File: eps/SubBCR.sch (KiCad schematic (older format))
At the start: 30 parts, among them Q44 IRF7425, Q45 IRF7425, U23 LT6106, U25 LT6106, U26 LTC4412xS6, U30 LTC4412xS6, U31 LT3652EMSE, U32 ADA4807-2ARM

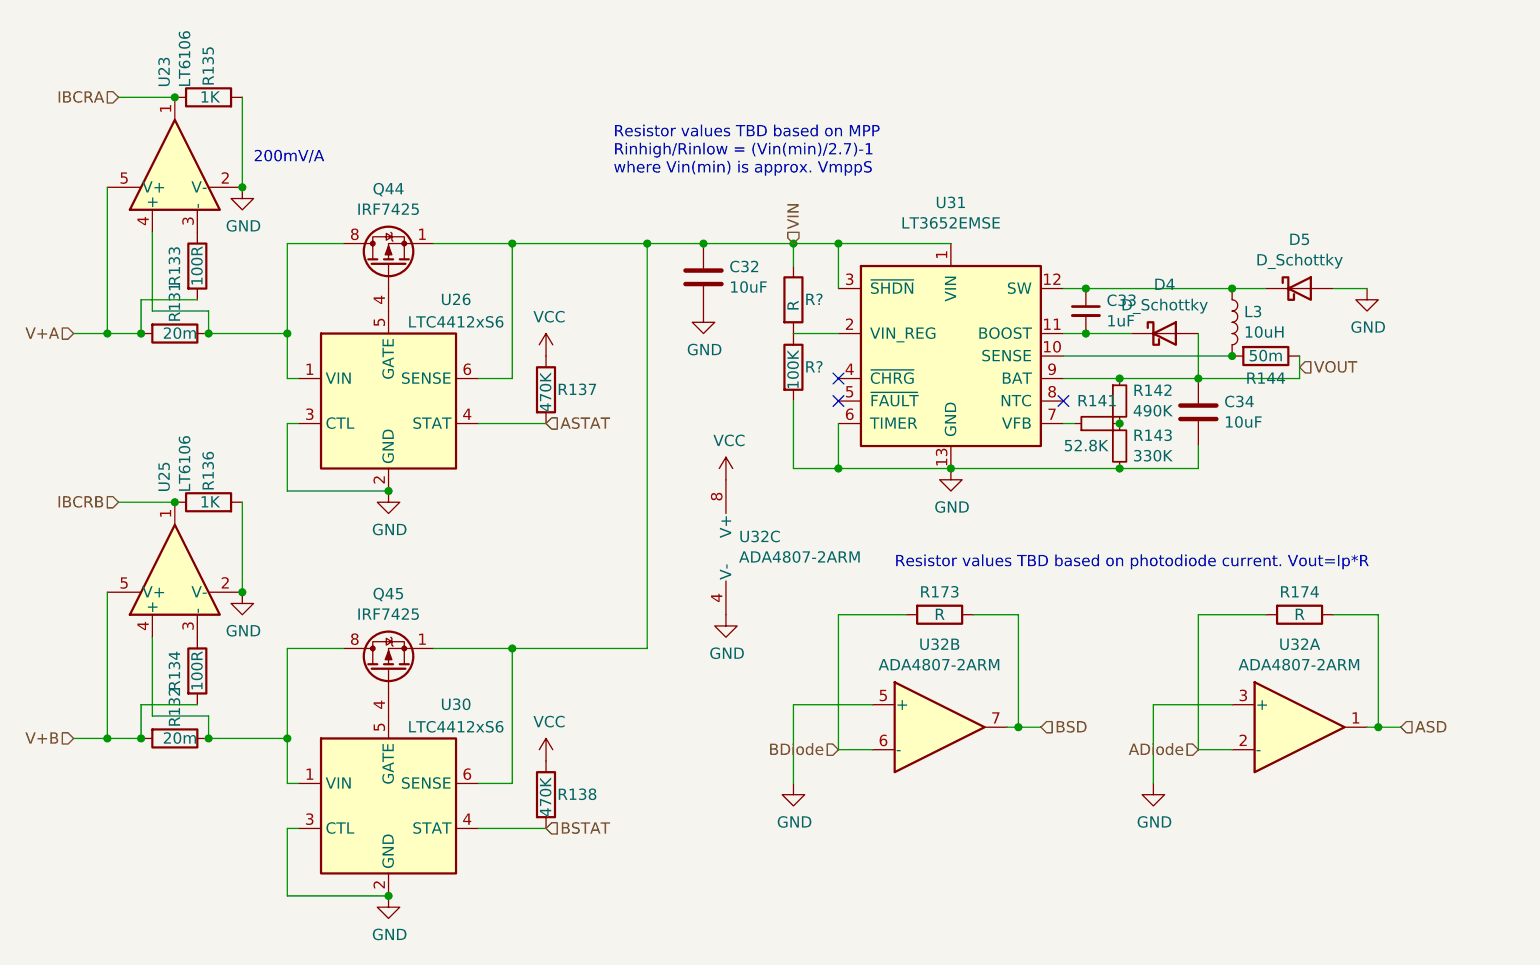
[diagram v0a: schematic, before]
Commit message: implement PDM LCLs
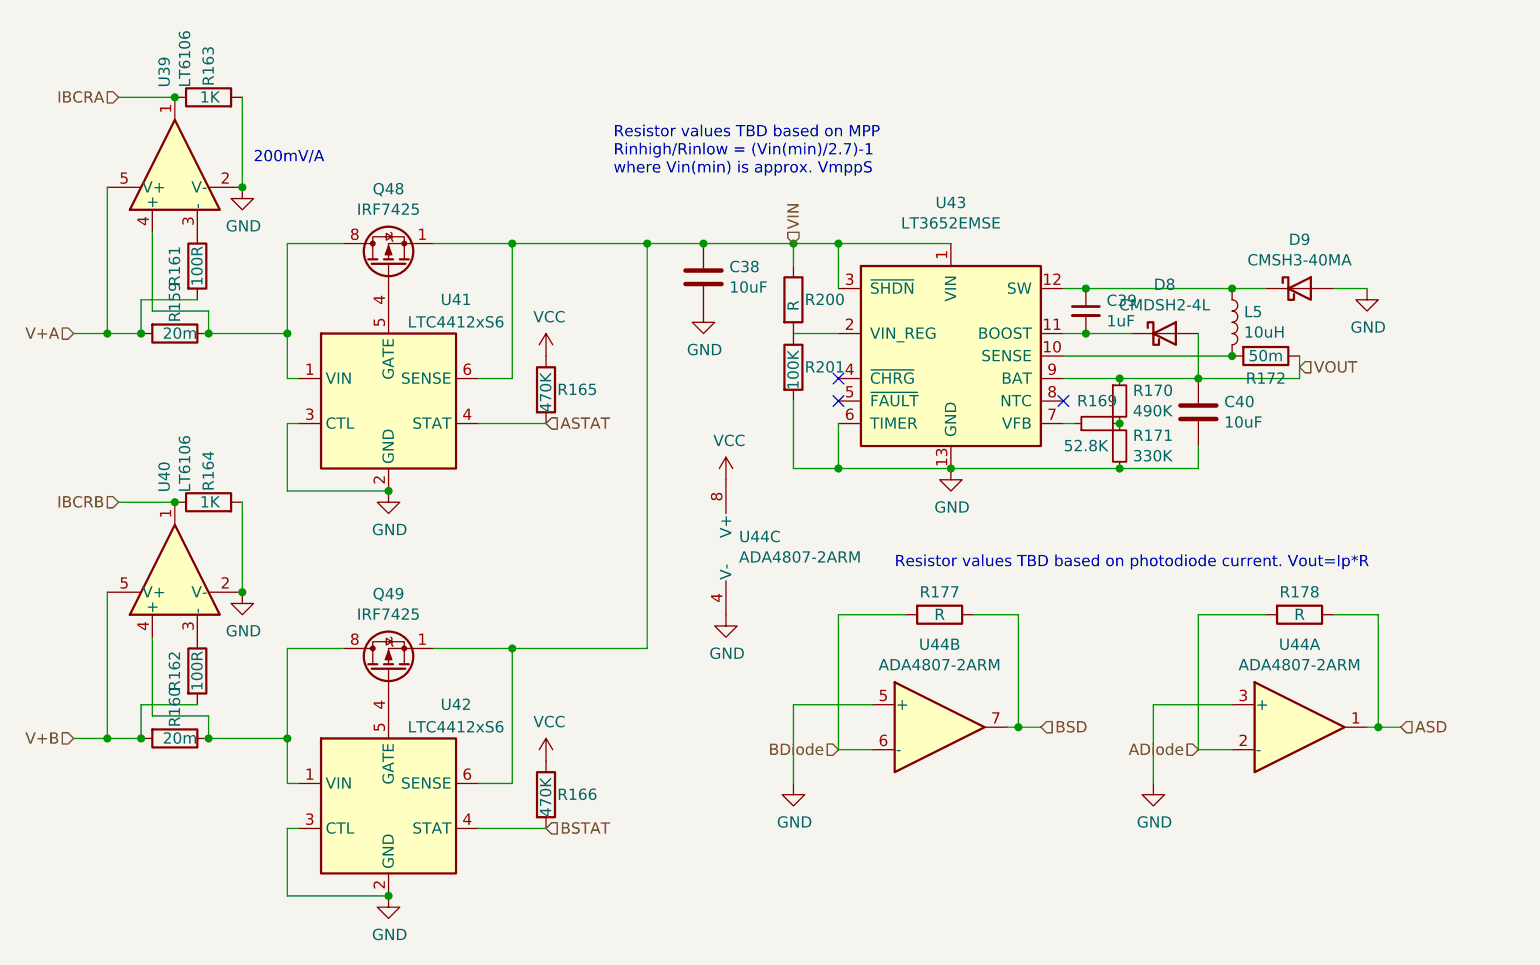
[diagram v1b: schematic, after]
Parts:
- D4: value D_Schottky -> CMDSH2-4L
- D5: value D_Schottky -> CMSH3-40MA
- gave numbers to parts that had none: 2

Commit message: update pcbnew
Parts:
- C32, C33, C34: footprint (none) -> Capacitor_SMD:C_0805_2012Metric_Pad1.18x1.45mm_HandSolder
- R131, R132, R133, R134, R135, R136, R137, R138, R141, R142, R143, R144, R175, R176, R196, R197: footprint (none) -> Resistor_SMD:R_0805_2012Metric_Pad1.20x1.40mm_HandSolder
